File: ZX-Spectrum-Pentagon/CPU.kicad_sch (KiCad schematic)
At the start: 17 parts, among them U2 74HC14, U24 74HC245, U25 74HC541, U26 74HC541, U27 Z80CPU, U28 74HC244, U29 GAL16V8, U30 29F040, U31 74HC32, U49 74HC08

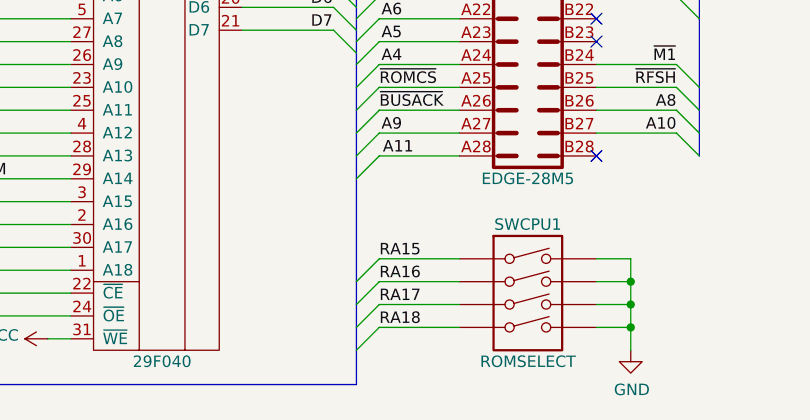
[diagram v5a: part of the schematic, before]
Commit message: change order of rom select
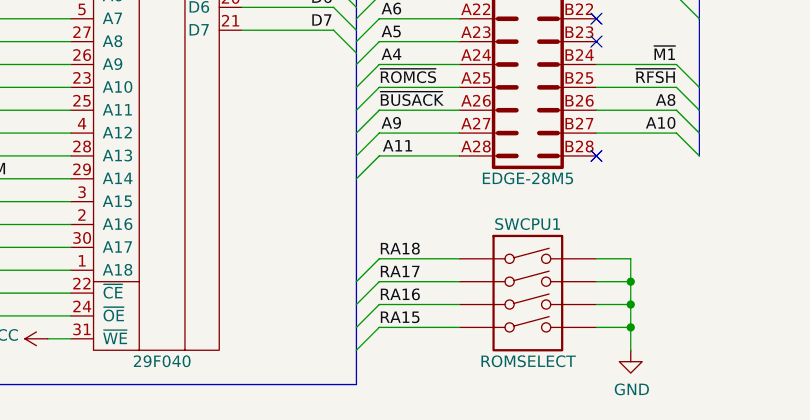
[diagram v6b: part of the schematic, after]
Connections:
- net RA15: now also SWCPU1.4; no longer SWCPU1.1
- net RA16: now also SWCPU1.3; no longer SWCPU1.2
- net RA17: now also SWCPU1.2; no longer SWCPU1.3
- net RA18: now also SWCPU1.1; no longer SWCPU1.4
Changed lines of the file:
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@@
     (effects (font (size 1.27 1.27)) (justify left bottom))
   )
-  (label "RA15" (at 138.43 170.18 0)
+  (label "RA15" (at 138.43 177.8 0)
     (effects (font (size 1.27 1.27)) (justify left bottom))
   )
@@
     (effects (font (size 1.27 1.27)) (justify left bottom))
   )
-  (label "RA17" (at 138.43 175.26 0)
+  (label "RA17" (at 138.43 172.72 0)
     (effects (font (size 1.27 1.27)) (justify left bottom))
   )
@@
     (effects (font (size 1.27 1.27)) (justify left bottom))
   )
-  (label "RA16" (at 138.43 172.72 0)
+  (label "RA16" (at 138.43 175.26 0)
     (effects (font (size 1.27 1.27)) (justify left bottom))
   )
@@
     (effects (font (size 1.27 1.27)) (justify left bottom))
   )
-  (label "RA18" (at 138.43 177.8 0)
-    (effects (font (size 1.27 1.27)) (justify left bottom))
-  )
+  (label "RA18" (at 138.43 170.18 0)
+    (effects (font (size 1.27 1.27)) (justify left bottom))
+  )

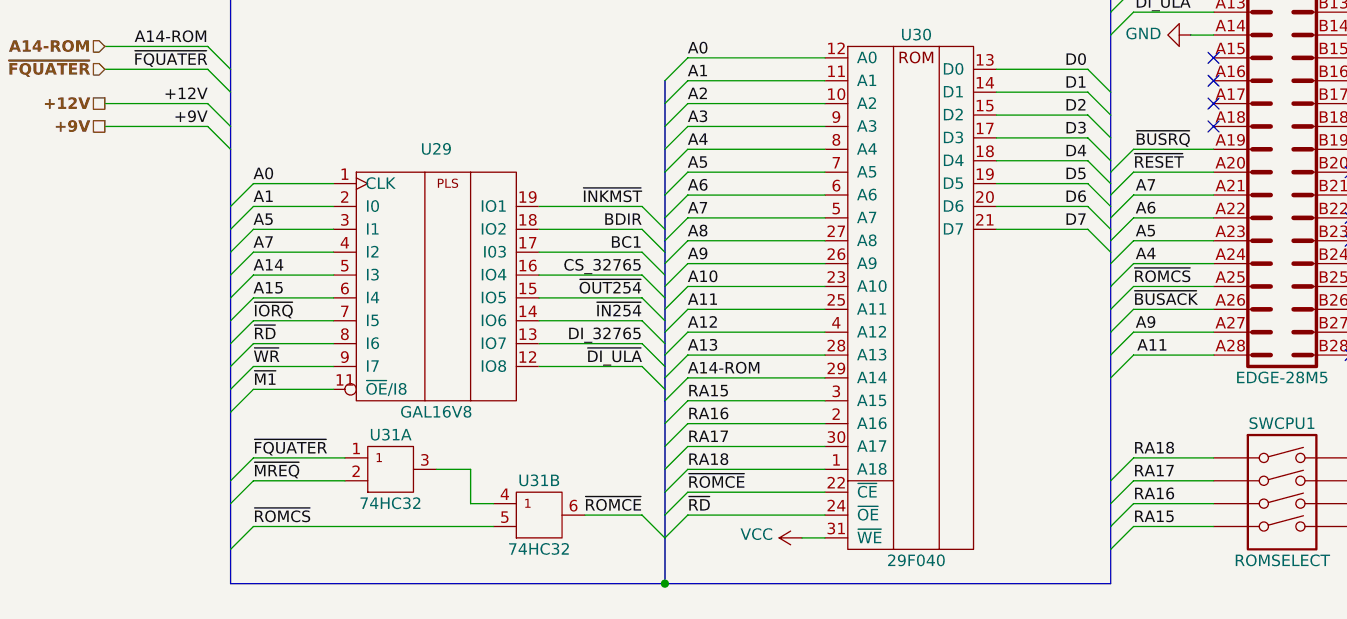
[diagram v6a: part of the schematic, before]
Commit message: reconect port address decocer tracing
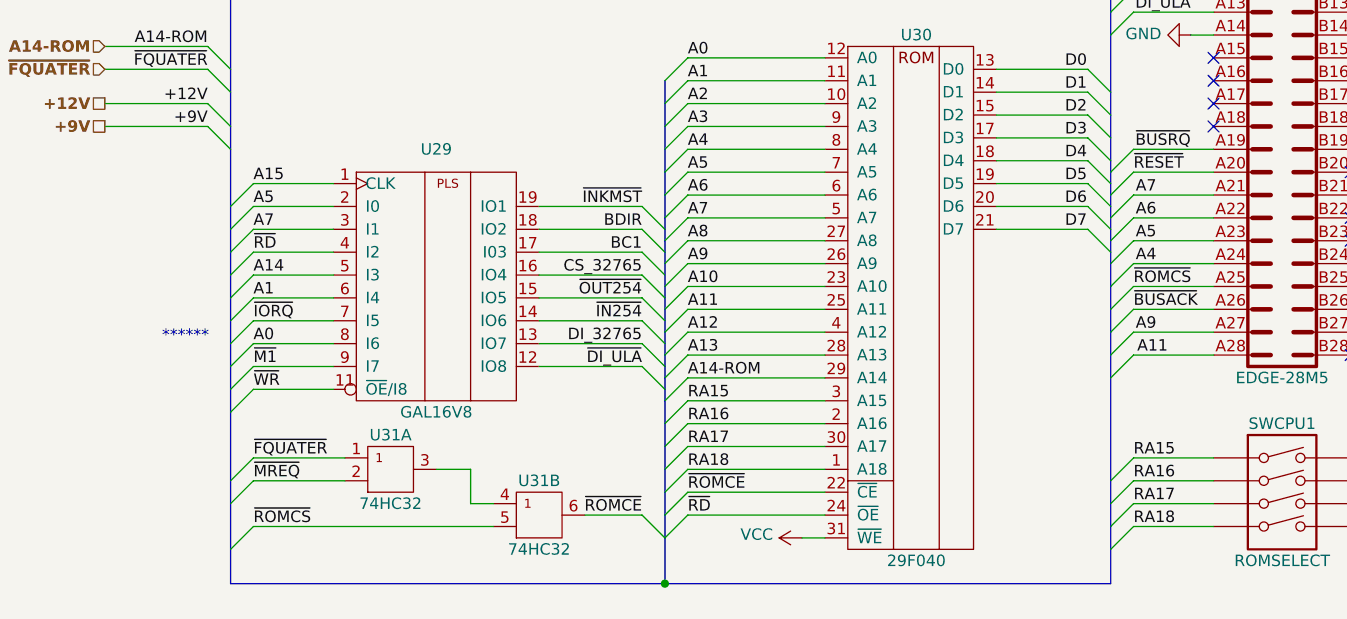
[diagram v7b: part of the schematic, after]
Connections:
- net A0: now also U29.8 (I6); no longer U29.1 (CLK)
- net A1: now also U29.6 (I4); no longer U29.2 (I0)
- net A15: now also U29.1 (CLK); no longer U29.6 (I4)
- net A5: now also U29.2 (I0); no longer U29.3 (I1)
- net A7: now also U29.3 (I1); no longer U29.4 (I2)
- net RA15: now also SWCPU1.1; no longer SWCPU1.4
- net RA16: now also SWCPU1.2; no longer SWCPU1.3
- net RA17: now also SWCPU1.3; no longer SWCPU1.2
- net RA18: now also SWCPU1.4; no longer SWCPU1.1
- net ~{M1}: now also U29.9 (I7); no longer U29.11 (~{OE}/I8)
- net ~{RD}: now also U29.4 (I2); no longer U29.8 (I6)
- net ~{WR}: now also U29.11 (~{OE}/I8); no longer U29.9 (I7)
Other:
- note added: "******"
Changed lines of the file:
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@@
     (effects (font (size 1.27 1.27) (thickness 0.254) bold) (justify right bottom))
+  )
+  (text "******" (at 30.48 157.48 0)
+    (effects (font (size 1.27 1.27)) (justify left bottom))
   )
   (text "TOP" (at 165.1 87.63 180)
@@
     (effects (font (size 1.27 1.27)) (justify right bottom))
   )
-  (label "~{RD}" (at 40.64 157.48 0)
+  (label "~{RD}" (at 40.64 147.32 0)
     (effects (font (size 1.27 1.27)) (justify left bottom))
   )
@@
     (effects (font (size 1.27 1.27)) (justify left bottom))
   )
-  (label "A5" (at 40.64 144.78 0)
+  (label "A5" (at 40.64 142.24 0)
     (effects (font (size 1.27 1.27)) (justify left bottom))
   )
@@
     (effects (font (size 1.27 1.27)) (justify left bottom))
   )
-  (label "RA15" (at 138.43 177.8 0)
+  (label "RA15" (at 138.43 170.18 0)
     (effects (font (size 1.27 1.27)) (justify left bottom))
   )
@@
     (effects (font (size 1.27 1.27)) (justify left bottom))
   )
-  (label "A1" (at 40.64 142.24 0)
+  (label "A1" (at 40.64 152.4 0)
     (effects (font (size 1.27 1.27)) (justify left bottom))
   )
@@
     (effects (font (size 1.27 1.27)) (justify left bottom))
   )
-  (label "A15" (at 40.64 152.4 0)
+  (label "A15" (at 40.64 139.7 0)
     (effects (font (size 1.27 1.27)) (justify left bottom))
   )
@@
     (effects (font (size 1.27 1.27)) (justify left bottom))
   )
-  (label "~{WR}" (at 40.64 160.02 0)
+  (label "~{WR}" (at 40.64 162.56 0)
     (effects (font (size 1.27 1.27)) (justify left bottom))
   )
@@
     (effects (font (size 1.27 1.27)) (justify right bottom))
   )
-  (label "~{M1}" (at 40.64 162.56 0)
+  (label "~{M1}" (at 40.64 160.02 0)
     (effects (font (size 1.27 1.27)) (justify left bottom))
   )
@@
     (effects (font (size 1.27 1.27)) (justify left bottom))
   )
-  (label "RA17" (at 138.43 172.72 0)
+  (label "RA17" (at 138.43 175.26 0)
     (effects (font (size 1.27 1.27)) (justify left bottom))
   )
@@
     (effects (font (size 1.27 1.27)) (justify left bottom))
   )
-  (label "A7" (at 40.64 147.32 0)
+  (label "A7" (at 40.64 144.78 0)
     (effects (font (size 1.27 1.27)) (justify left bottom))
   )
@@
     (effects (font (size 1.27 1.27)) (justify right bottom))
   )
-  (label "A0" (at 40.64 139.7 0)
+  (label "A0" (at 40.64 157.48 0)
     (effects (font (size 1.27 1.27)) (justify left bottom))
   )
@@
     (effects (font (size 1.27 1.27)) (justify left bottom))
   )
-  (label "RA16" (at 138.43 175.26 0)
+  (label "RA16" (at 138.43 172.72 0)
     (effects (font (size 1.27 1.27)) (justify left bottom))
   )
@@
     (effects (font (size 1.27 1.27)) (justify left bottom))
   )
-  (label "RA18" (at 138.43 170.18 0)
-    (effects (font (size 1.27 1.27)) (justify left bottom))
-  )
+  (label "RA18" (at 138.43 177.8 0)
+    (effects (font (size 1.27 1.27)) (justify left bottom))
+  )

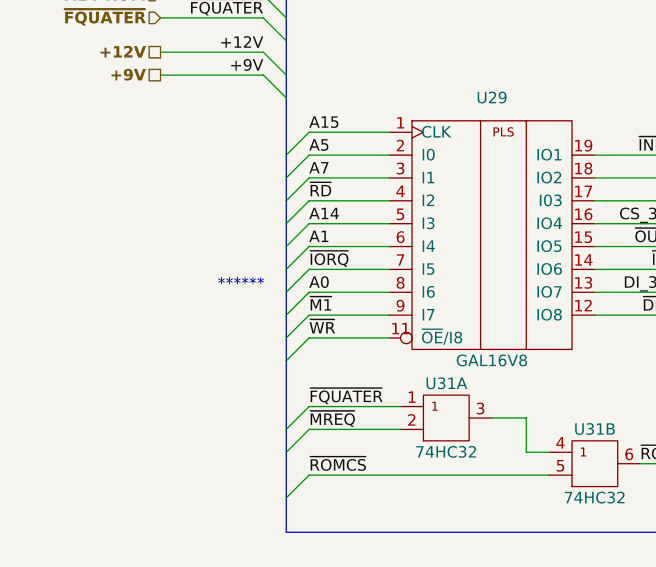
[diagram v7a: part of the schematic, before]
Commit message: reconnected address bus
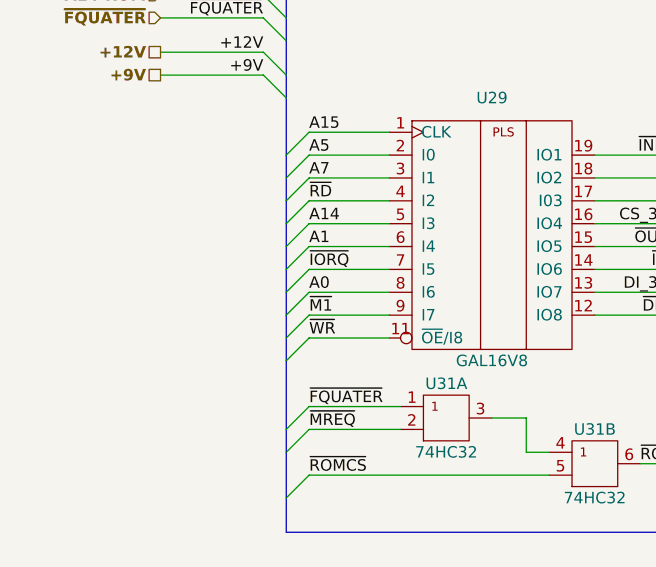
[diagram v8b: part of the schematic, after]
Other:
- note removed: "******"
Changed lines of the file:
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@@
     (effects (font (size 1.27 1.27) (thickness 0.254) bold) (justify right bottom))
-  )
-  (text "******" (at 30.48 157.48 0)
-    (effects (font (size 1.27 1.27)) (justify left bottom))
   )
   (text "TOP" (at 165.1 87.63 180)
